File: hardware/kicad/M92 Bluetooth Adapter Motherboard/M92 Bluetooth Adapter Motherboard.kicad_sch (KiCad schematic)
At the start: 26 parts, among them IC1 PIC18F27Q43-I/SO, J2 Conn_Handset_RJ45, J6 Conn_MCU_Programming, J7 Conn_BT_Module, J8 Conn_MCU_IO_UART, Q2 PN2222ATA

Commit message: Update battery voltage divider to use larger resistor values
Increase voltage divider resistor values to reduce current draw.  Since I am never switching ADC input pins on the MCU and sampling rate is very low (once per 5 seconds), the very high impedance does not appear to impact ADC reading accuracy. I also found that the 10nF capacitor was unnecessary, so that is now removed.

Also updated JLCPCB part numbers for several resistors and capacitors to use "basic" parts instead of "extended" parts.
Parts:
- C18, C19, C24: JLCPCB Part # C5137650 -> C24497
- R17, R22: JLCPCB Part # C212479 -> C17902
- R18, R20: JLCPCB Part # C212494 -> C17944
- R19: JLCPCB Part # C102060 -> C4410
- R21: JLCPCB Part # C212480 -> C17900
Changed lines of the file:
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@@
       (effects (font (size 1.27 1.27)) hide)
     )
-    (property "JLCPCB Part #" "C102060" (at 226.06 85.09 0)
+    (property "JLCPCB Part #" "C4410" (at 226.06 85.09 0)
       (effects (font (size 1.27 1.27)) hide)
     )
@@
       (effects (font (size 1.27 1.27)) hide)
     )
-    (property "JLCPCB Part #" "C212479" (at 76.2 33.02 0)
+    (property "JLCPCB Part #" "C17902" (at 76.2 33.02 0)
       (effects (font (size 1.27 1.27)) hide)
     )
@@
       (effects (font (size 1.27 1.27)) hide)
     )
-    (property "JLCPCB Part #" "C212494" (at 229.87 92.71 0)
+    (property "JLCPCB Part #" "C17944" (at 229.87 92.71 0)
       (effects (font (size 1.27 1.27)) hide)
     )
@@
       (effects (font (size 1.27 1.27)) hide)
     )
-    (property "JLCPCB Part #" "C5137650" (at 96.52 153.67 0)
+    (property "JLCPCB Part #" "C24497" (at 96.52 153.67 0)
       (effects (font (size 1.27 1.27)) hide)
     )
@@
       (effects (font (size 1.27 1.27)) hide)
     )
-    (property "JLCPCB Part #" "C5137650" (at 135.89 78.74 0)
+    (property "JLCPCB Part #" "C24497" (at 135.89 78.74 0)
       (effects (font (size 1.27 1.27)) hide)
     )
@@
       (effects (font (size 1.27 1.27)) hide)
     )
-    (property "JLCPCB Part #" "C212494" (at 240.03 46.99 0)
+    (property "JLCPCB Part #" "C17944" (at 240.03 46.99 0)
       (effects (font (size 1.27 1.27)) hide)
     )
@@
       (effects (font (size 1.27 1.27)) hide)
     )
-    (property "JLCPCB Part #" "C212479" (at 223.52 39.37 0)
+    (property "JLCPCB Part #" "C17902" (at 223.52 39.37 0)
       (effects (font (size 1.27 1.27)) hide)
     )
@@
       (effects (font (size 1.27 1.27)) hide)
     )
-    (property "JLCPCB Part #" "C5137650" (at 207.01 147.32 0)
+    (property "JLCPCB Part #" "C24497" (at 207.01 147.32 0)
       (effects (font (size 1.27 1.27)) hide)
     )
@@
       (effects (font (size 1.27 1.27)) hide)
     )
-    (property "JLCPCB Part #" "C212480" (at 246.38 121.92 0)
-      (effects (font (size 1.27 1.27)) hide)
-    )
+    (property "JLCPCB Part #" "C17900" (at 246.38 121.92 0)
+      (effects (font (size 1.27 1.27)) hide)
+    )

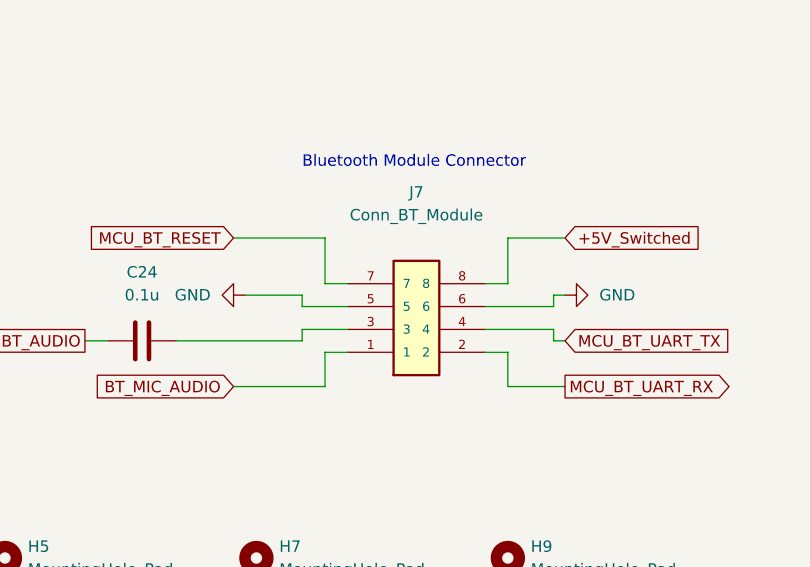
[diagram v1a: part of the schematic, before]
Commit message: Create new symbol/footprint for original 8-pin header on transceiver PCB
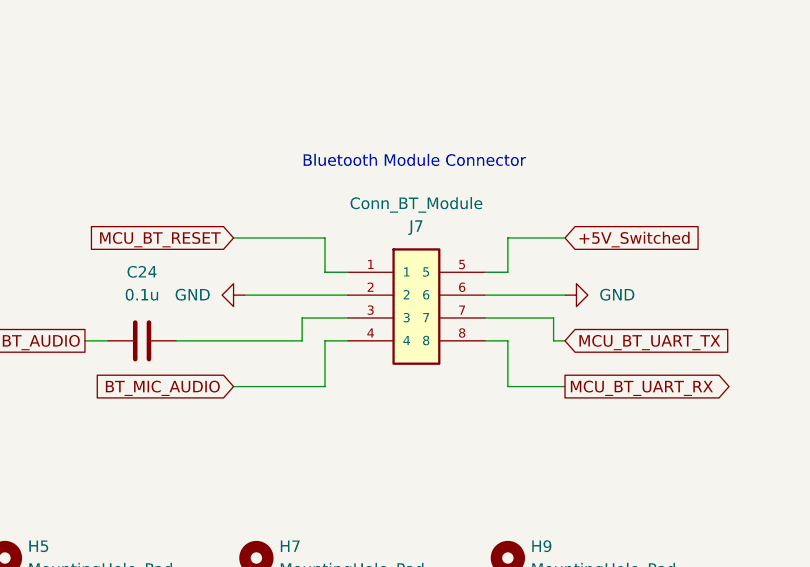
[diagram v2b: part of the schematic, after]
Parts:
- J7: footprint M92 Bluetooth Adapter Motherboard:SAMTEC_ESW-104-44-T-D -> M92 Bluetooth Adapter Motherboard:JAE_DRA-8SC-F0; symbol M92 Bluetooth Adapter Motherboard:ESW-104-44-T-D -> M92 Bluetooth Adapter Motherboard:JAE_DRA-8SC-F0; Manufacturer_Name Samtec -> JAE; Manufacturer_Part_Number ESW-104-44-T-D -> DRA-8SC-F0
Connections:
- net +5V_Switched: now also J7.5; no longer J7.8
- net BT_MIC_AUDIO: now also J7.4; no longer J7.1
- net GND: now also J7.2; no longer J7.5
- net MCU_BT_RESET: now also J7.1; no longer J7.7
- net MCU_BT_UART_RX: now also J7.8; no longer J7.2
- net MCU_BT_UART_TX: now also J7.7; no longer J7.4
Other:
- moved on the sheet: J7
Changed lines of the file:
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@@
     (stroke (width 0) (type default))
   )
-  (wire (pts (xy 116.84 147.32) (xy 116.84 142.24))
+  (wire (pts (xy 116.84 146.05) (xy 116.84 142.24))
     (stroke (width 0) (type default))
   )
@@
     (stroke (width 0) (type default))
   )
-  (wire (pts (xy 116.84 147.32) (xy 119.38 147.32))
-    (stroke (width 0) (type default))
-  )
-  (wire (pts (xy 142.24 149.86) (xy 142.24 148.59))
-    (stroke (width 0) (type default))
-  )
   (wire (pts (xy 58.42 53.34) (xy 68.58 53.34))
     (stroke (width 0) (type default))
@@
     (stroke (width 0) (type default))
   )
+  (wire (pts (xy 134.62 146.05) (xy 137.16 146.05))
+    (stroke (width 0) (type default))
+  )
   (wire (pts (xy 71.12 59.69) (xy 76.2 59.69))
     (stroke (width 0) (type default))
@@
     (stroke (width 0) (type default))
   )
+  (wire (pts (xy 134.62 151.13) (xy 142.24 151.13))
+    (stroke (width 0) (type default))
+  )
   (wire (pts (xy 240.03 134.62) (xy 250.19 134.62))
     (stroke (width 0) (type default))
   )
-  (wire (pts (xy 137.16 147.32) (xy 134.62 147.32))
-    (stroke (width 0) (type default))
-  )
   (wire (pts (xy 124.46 57.15) (xy 127 57.15))
     (stroke (width 0) (type default))
@@
     (stroke (width 0) (type default))
   )
-  (wire (pts (xy 134.62 154.94) (xy 137.16 154.94))
+  (wire (pts (xy 134.62 153.67) (xy 137.16 153.67))
     (stroke (width 0) (type default))
   )
@@
     (stroke (width 0) (type default))
   )
-  (wire (pts (xy 114.3 148.59) (xy 107.95 148.59))
+  (wire (pts (xy 107.95 148.59) (xy 119.38 148.59))
     (stroke (width 0) (type default))
   )
@@
     (stroke (width 0) (type default))
   )
-  (wire (pts (xy 116.84 154.94) (xy 116.84 158.75))
+  (wire (pts (xy 116.84 153.67) (xy 116.84 158.75))
     (stroke (width 0) (type default))
   )
@@
     (stroke (width 0) (type default))
   )
-  (wire (pts (xy 114.3 149.86) (xy 114.3 148.59))
-    (stroke (width 0) (type default))
-  )
   (wire (pts (xy 135.89 74.93) (xy 138.43 74.93))
     (stroke (width 0) (type default))
@@
     (stroke (width 0) (type default))
   )
-  (wire (pts (xy 142.24 148.59) (xy 143.51 148.59))
-    (stroke (width 0) (type default))
-  )
   (wire (pts (xy 133.35 83.82) (xy 135.89 83.82))
     (stroke (width 0) (type default))
@@
     (stroke (width 0) (type default))
   )
-  (wire (pts (xy 137.16 142.24) (xy 137.16 147.32))
+  (wire (pts (xy 137.16 142.24) (xy 137.16 146.05))
     (stroke (width 0) (type default))
   )
@@
     (stroke (width 0) (type default))
   )
-  (wire (pts (xy 116.84 154.94) (xy 119.38 154.94))
+  (wire (pts (xy 116.84 153.67) (xy 119.38 153.67))
     (stroke (width 0) (type default))
   )
@@
     (stroke (width 0) (type default))
   )
+  (wire (pts (xy 116.84 146.05) (xy 119.38 146.05))
+    (stroke (width 0) (type default))
+  )
   (wire (pts (xy 127 38.1) (xy 104.14 38.1))
     (stroke (width 0) (type default))
   )
-  (wire (pts (xy 142.24 152.4) (xy 142.24 153.67))
+  (wire (pts (xy 142.24 151.13) (xy 142.24 153.67))
     (stroke (width 0) (type default))
   )
@@
     (stroke (width 0) (type default))
   )
-  (wire (pts (xy 114.3 153.67) (xy 114.3 152.4))
+  (wire (pts (xy 114.3 151.13) (xy 114.3 153.67))
     (stroke (width 0) (type default))
   )
@@
     (stroke (width 0) (type default))
   )
-  (wire (pts (xy 134.62 149.86) (xy 142.24 149.86))
-    (stroke (width 0) (type default))
-  )
   (wire (pts (xy 240.03 43.18) (xy 240.03 39.37))
     (stroke (width 0) (type default))
@@
     (stroke (width 0) (type default))
   )
-  (wire (pts (xy 137.16 158.75) (xy 137.16 154.94))
+  (wire (pts (xy 137.16 158.75) (xy 137.16 153.67))
     (stroke (width 0) (type default))
   )
@@
     (stroke (width 0) (type default))
   )
+  (wire (pts (xy 114.3 151.13) (xy 119.38 151.13))
+    (stroke (width 0) (type default))
+  )
   (wire (pts (xy 213.36 132.08) (xy 219.71 132.08))
     (stroke (width 0) (type default))
@@
     (stroke (width 0) (type default))
   )
-  (wire (pts (xy 134.62 152.4) (xy 142.24 152.4))
-    (stroke (width 0) (type default))
-  )
-  (wire (pts (xy 114.3 152.4) (xy 119.38 152.4))
-    (stroke (width 0) (type default))
-  )
   (wire (pts (xy 132.08 53.34) (xy 132.08 62.23))
     (stroke (width 0) (type default))
@@
     (stroke (width 0) (type default))
   )
-  (wire (pts (xy 114.3 149.86) (xy 119.38 149.86))
+  (wire (pts (xy 134.62 148.59) (xy 143.51 148.59))
     (stroke (width 0) (type default))
   )
@@
     )
   )
-  (symbol (lib_id "M92 Bluetooth Adapter Motherboard:ESW-104-44-T-D") (at 127 149.86 0) (mirror x) (unit 1)
+  (symbol (lib_id "M92 Bluetooth Adapter Motherboard:JAE_DRA-8SC-F0") (at 127 151.13 0) (unit 1)
     (in_bom yes) (on_board yes) (dnp no)
-    (property "Reference" "J7" (at 127 137.16 0)
-      (effects (font (size 1.27 1.27)))
-    )
-    (property "Value" "Conn_BT_Module" (at 127 139.7 0)
-      (effects (font (size 1.27 1.27)))
-    )
-    (property "Footprint" "M92 Bluetooth Adapter Motherboard:SAMTEC_ESW-104-44-T-D" (at 127 149.86 0)
+    (property "Reference" "J7" (at 127 140.97 0)
+      (effects (font (size 1.27 1.27)))
+    )
+    (property "Value" "Conn_BT_Module" (at 127 138.43 0)
+      (effects (font (size 1.27 1.27)))
+    )
+    (property "Footprint" "M92 Bluetooth Adapter Motherboard:JAE_DRA-8SC-F0" (at 127 151.13 0)
       (effects (font (size 1.27 1.27)) (justify bottom) hide)
     )
-    (property "Datasheet" "https://www.mouser.com/datasheet/2/527/esq_th-1369982.pdf" (at 127 149.86 0)
-      (effects (font (size 1.27 1.27)) hide)
-    )
-    (property "Manufacturer_Name" "Samtec" (at 127 149.86 0)
-      (effects (font (size 1.27 1.27)) (justify bottom) hide)
-    )
-    (property "Manufacturer_Part_Number" "ESW-104-44-T-D" (at 127 149.86 0)
-      (effects (font (size 1.27 1.27)) hide)
-    )
-    (property "Mouser Part Number" "200-ESW-104-44-T-D" (at 127 149.86 0)
-      (effects (font (size 1.27 1.27)) hide)
-    )
-    (property "Mouser Price/Stock" "https://www.mouser.com/ProductDetail/200-ESW10444TD" (at 127 149.86 0)
-      (effects (font (size 1.27 1.27)) hide)
-    )
-    (property "JLCPCB Part #" "" (at 127 149.86 0)
-      (effects (font (size 1.27 1.27)) hide)
-    )
+    (property "Datasheet" "https://www.mouser.com/datasheet/2/527/esq_th-1369982.pdf" (at 127 151.13 0)
+      (effects (font (size 1.27 1.27)) hide)
+    )
+    (property "Manufacturer_Name" "JAE" (at 127 151.13 0)
+      (effects (font (size 1.27 1.27)) hide)
+    )
+    (property "Manufacturer_Part_Number" "DRA-8SC-F0" (at 127 151.13 0)
+      (effects (font (size 1.27 1.27)) hide)
+    )
+    (property "Mouser Part Number" "200-ESW-104-44-T-D" (at 127 151.13 0)
+      (effects (font (size 1.27 1.27)) hide)
+    )
+    (property "Mouser Price/Stock" "https://www.mouser.com/ProductDetail/200-ESW10444TD" (at 127 151.13 0)
+      (effects (font (size 1.27 1.27)) hide)
+    )
+    (property "JLCPCB Part #" "" (at 127 151.13 0)
+      (effects (font (size 1.27 1.27)) hide)
+    )

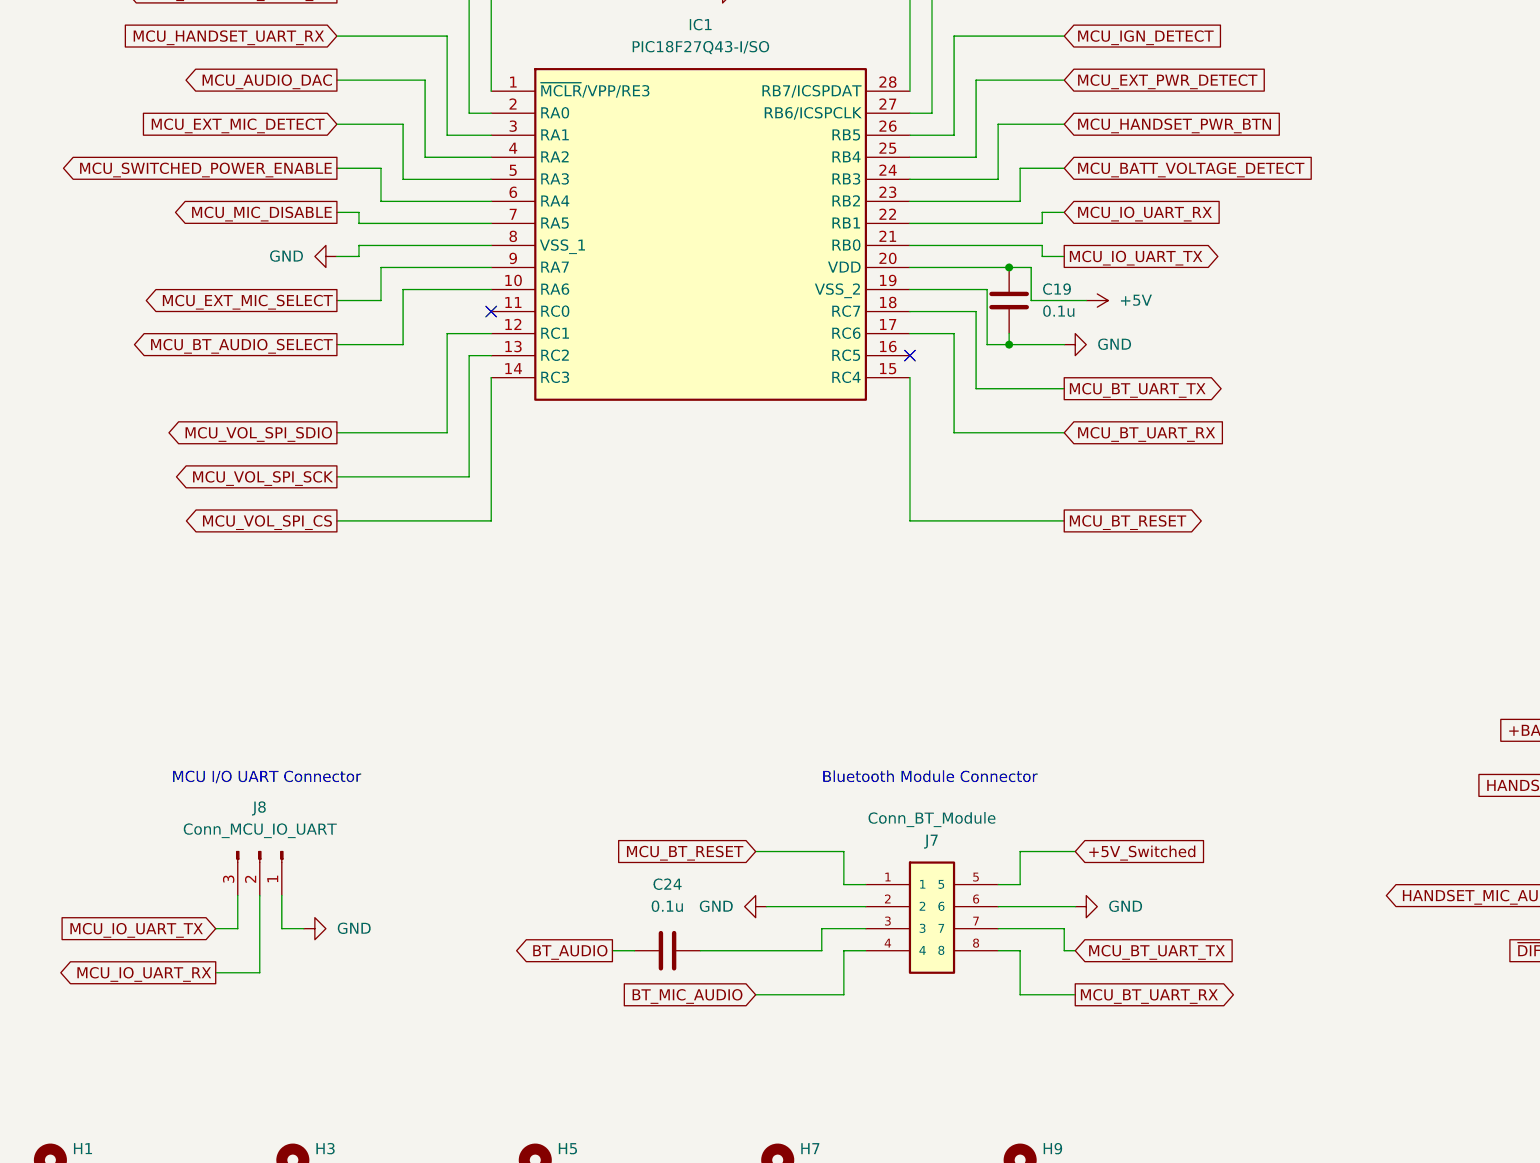
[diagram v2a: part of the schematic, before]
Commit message: Update circuit/PCB to use different power supply/switching components
* Use more efficient 5V regulator.
* Use load switch ICs instead of reed switch relays for power switching.
* Swapped MCU pins for battery voltage detect and power switching for better PCB layout.
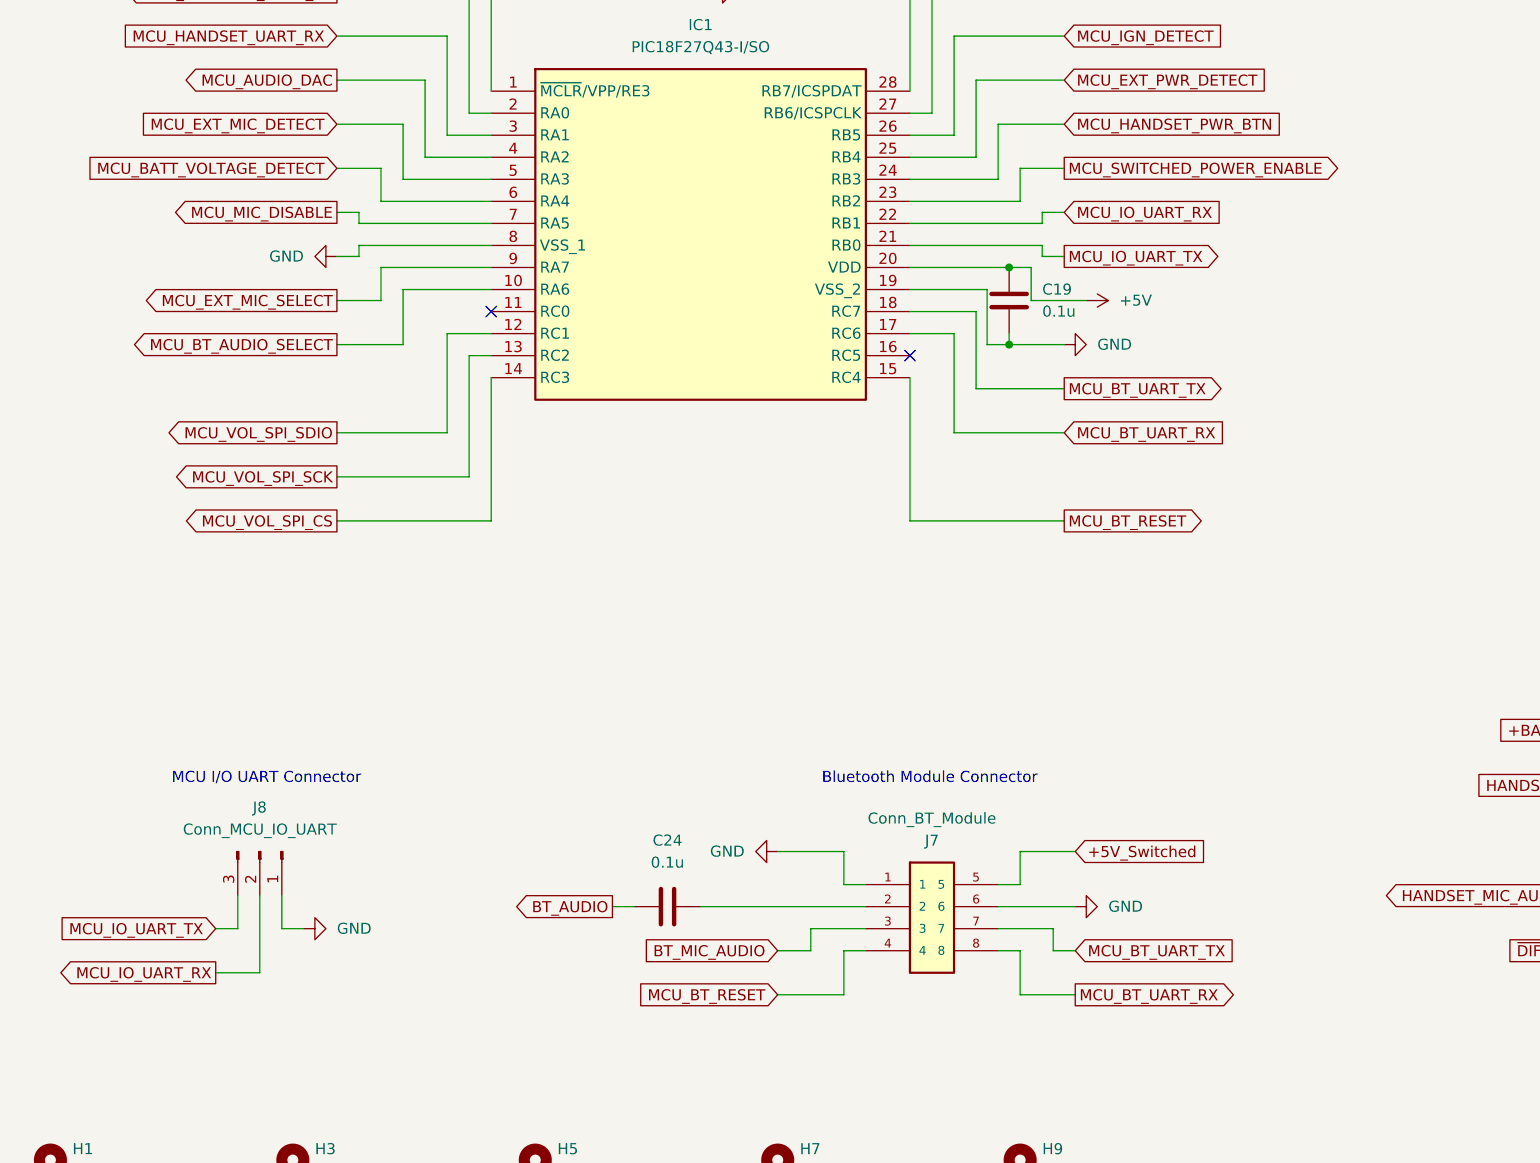
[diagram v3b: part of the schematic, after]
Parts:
- J7: Mouser Part Number 200-ESW-104-44-T-D -> (none); Mouser Price/Stock https://www.mouser.com/ProductDetail/200-ESW10444TD -> (none)
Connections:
- net BT_MIC_AUDIO: now also J7.3; no longer J7.4
- net GND: now also J7.1; no longer J7.2
- net MCU_BATT_VOLTAGE_DETECT: now also IC1.6 (RA4); no longer IC1.23 (RB2)
- net MCU_BT_RESET: now also J7.4; no longer J7.1
- net MCU_SWITCHED_POWER_ENABLE: now also IC1.23 (RB2); no longer IC1.6 (RA4)
- net at C24.2: now also J7.2; no longer J7.3
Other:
- moved on the sheet: C24
